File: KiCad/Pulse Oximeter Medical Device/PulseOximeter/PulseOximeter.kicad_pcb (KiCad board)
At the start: 4 copper layers, 0 parts

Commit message: Create PCB layout and check DRC
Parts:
- added A1: Arduino_Nano_v3.x, Module:Arduino_Nano, F.Cu at (141.5, 118.7)
- added C1: 100n, Capacitor_THT:C_Disc_D4.7mm_W2.5mm_P5.00mm, F.Cu at (158.3, 120.0)
- added C2: 100n, Capacitor_THT:C_Disc_D4.7mm_W2.5mm_P5.00mm, F.Cu at (158.3, 107.0)
- added C3: 100n, Capacitor_THT:C_Disc_D4.7mm_W2.5mm_P5.00mm, F.Cu at (158.3, 94.0)
- added D1: LED, LED_THT:LED_D3.0mm, F.Cu at (162.1, 79.5)
- added R1: 1K, Resistor_THT:R_Axial_DIN0207_L6.3mm_D2.5mm_P7.62mm_Horizontal, F.Cu at (163.3, 114.2)
- added R2: 1K, Resistor_THT:R_Axial_DIN0207_L6.3mm_D2.5mm_P7.62mm_Horizontal, F.Cu at (163.3, 101.2)
- added R3: 1K, Resistor_THT:R_Axial_DIN0207_L6.3mm_D2.5mm_P7.62mm_Horizontal, F.Cu at (163.3, 87.7)
- added R4: 1K, Resistor_THT:R_Axial_DIN0207_L6.3mm_D2.5mm_P7.62mm_Horizontal, F.Cu at (147.7, 79.5)
- added SW1: SW_Push, Button_Switch_THT:SW_PUSH_6mm, F.Cu at (147.1, 115.2)
- added SW2: SW_Push, Button_Switch_THT:SW_PUSH_6mm, F.Cu at (147.1, 102.2)
- added SW3: SW_Push, Button_Switch_THT:SW_PUSH_6mm, F.Cu at (146.8, 89.2)
- added U1: MAX30102, pso_lib:MAX30102_Module, F.Cu at (105.5, 115.6)
- added U2: SSD1306, pso_lib:SSD1306_Module, F.Cu at (105.5, 91.0)
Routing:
- net +5V: track 0.00 -> 141.7 mm, vias 0 -> 2
- net Net-(A1-A4): track 0.00 -> 83.5 mm
- net Net-(A1-A5): track 0.00 -> 56.2 mm
- net Net-(A1-D2): track 0.00 -> 32.0 mm
- net Net-(A1-D4): track 0.00 -> 30.7 mm
- net Net-(A1-D3): track 0.00 -> 23.0 mm
- net Net-(A1-D12): track 0.00 -> 7.71 mm
- net Net-(D1-A): track 0.00 -> 4.23 mm
- added copper zone on B.Cu, net GND
- added copper zone on F.Cu, net GND
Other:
- board outline added: 82 x 55 mm

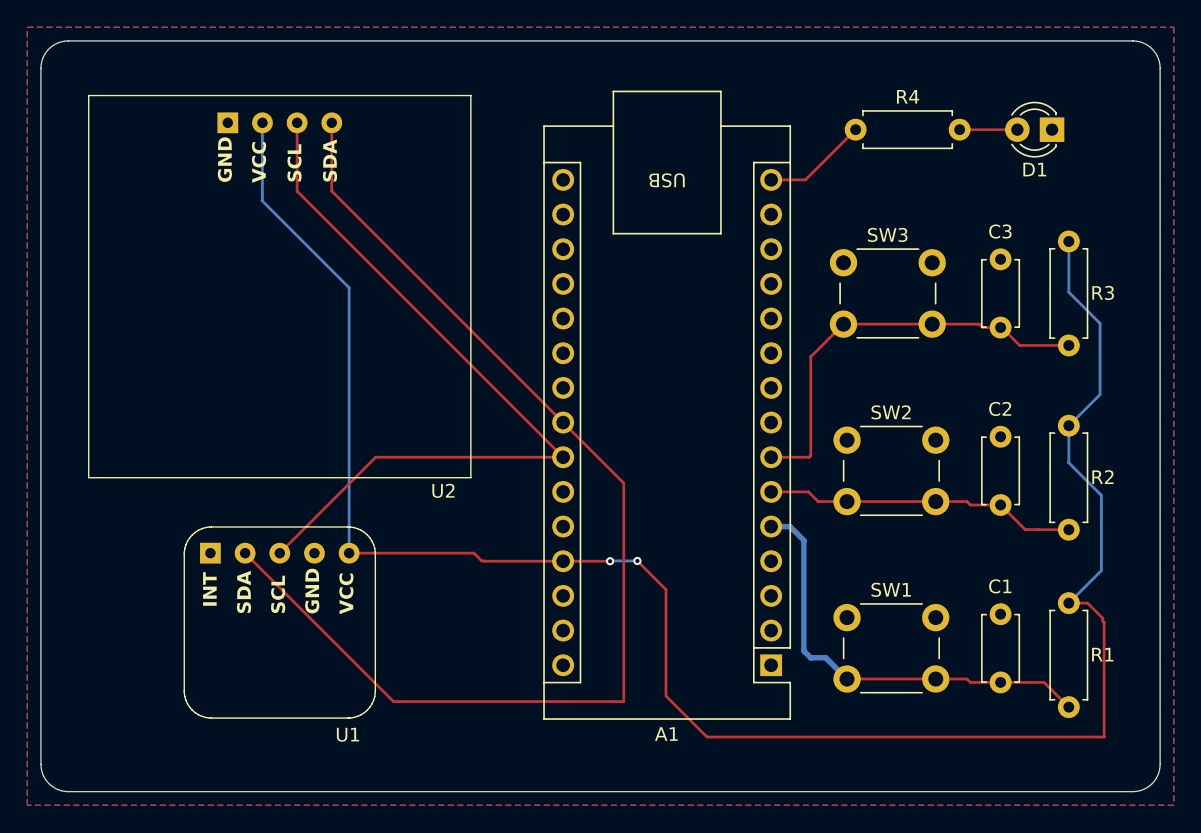
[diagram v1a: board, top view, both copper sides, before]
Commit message: Edit silkscreen text layer
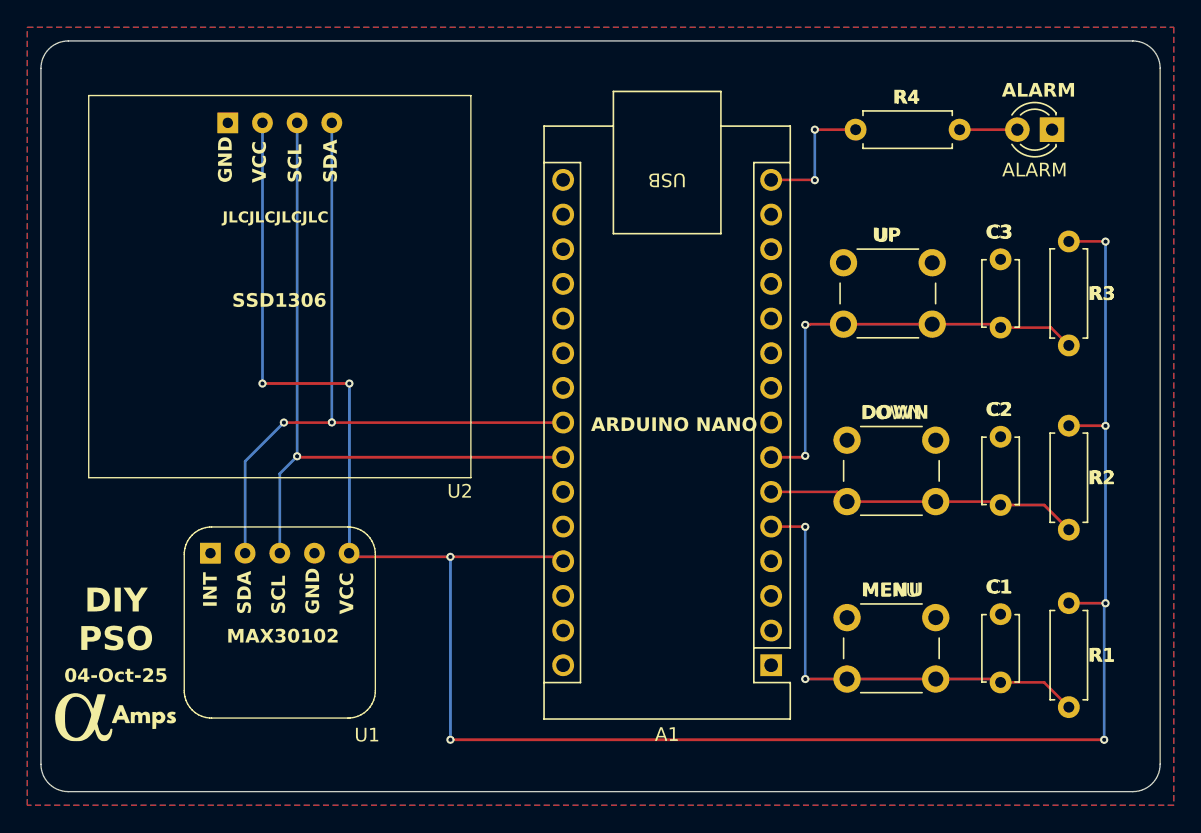
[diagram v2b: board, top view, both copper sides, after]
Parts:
- added G***: LOGO, LOGO, F.Cu at (93.5, 122.5)
- renumbered D1 to ALARM, SW2 to DOWN, SW1 to MENU, SW3 to UP
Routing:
- net Net-(A1-A4): track 83.5 -> 53.2 mm, vias 0 -> 2
- net +5V: track 141.7 -> 159.8 mm, vias 2 -> 8
- net Net-(A1-A5): track 56.2 -> 51.6 mm, vias 0 -> 1
- net Net-(A1-D12): track 7.71 -> 9.90 mm, vias 0 -> 2
- net Net-(A1-D2): track 32.0 -> 33.8 mm, vias 0 -> 2
- net Net-(A1-D4): track 30.7 -> 32.1 mm, vias 0 -> 2
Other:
- board text added: "04-Oct-25"
- board text added: "ALARM"
- board text added: "ARDUINO NANO"
- board text added: "C1"
- board text added: "C2"
- board text added: "C3"
- board text added: "DIY PSO"
- board text added: "DOWN"
- board text added: "JLCJLCJLCJLC"
- board text added: "MAX30102"
- board text added: "MENU"
- board text added: "R1"
- board text added: "R2"
- board text added: "R3"
- board text added: "R4"
- board text added: "SSD1306"
- board text added: "UP"

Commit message: Add PCB mounting holes
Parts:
- added REF**: MountingHole_2.1mm, MountingHole:MountingHole_2.1mm, F.Cu at (90.3, 125.7)
- added REF**: MountingHole_2.1mm, MountingHole:MountingHole_2.1mm, F.Cu at (90.3, 75.3)
- added REF**: MountingHole_2.1mm, MountingHole:MountingHole_2.1mm, F.Cu at (167.7, 125.7)
- added REF**: MountingHole_2.1mm, MountingHole:MountingHole_2.1mm, F.Cu at (167.7, 75.3)
- moved G*** 2.00 mm to (93.5, 120.5)
